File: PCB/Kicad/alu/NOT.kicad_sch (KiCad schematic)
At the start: 3 parts, among them U7 74LS04, U8 74LS04, U9 74LS04

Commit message: UPDATE
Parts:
- removed unit 6 of U9
- removed unit 5 of U9
- added C14, C15, C16: 10n, symbol Device:C
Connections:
- net GND: now also C14.2, C15.2, C16.2
- net VCC: now also C14.1, C15.1, C16.1
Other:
- moved on the sheet: U7G, U9G

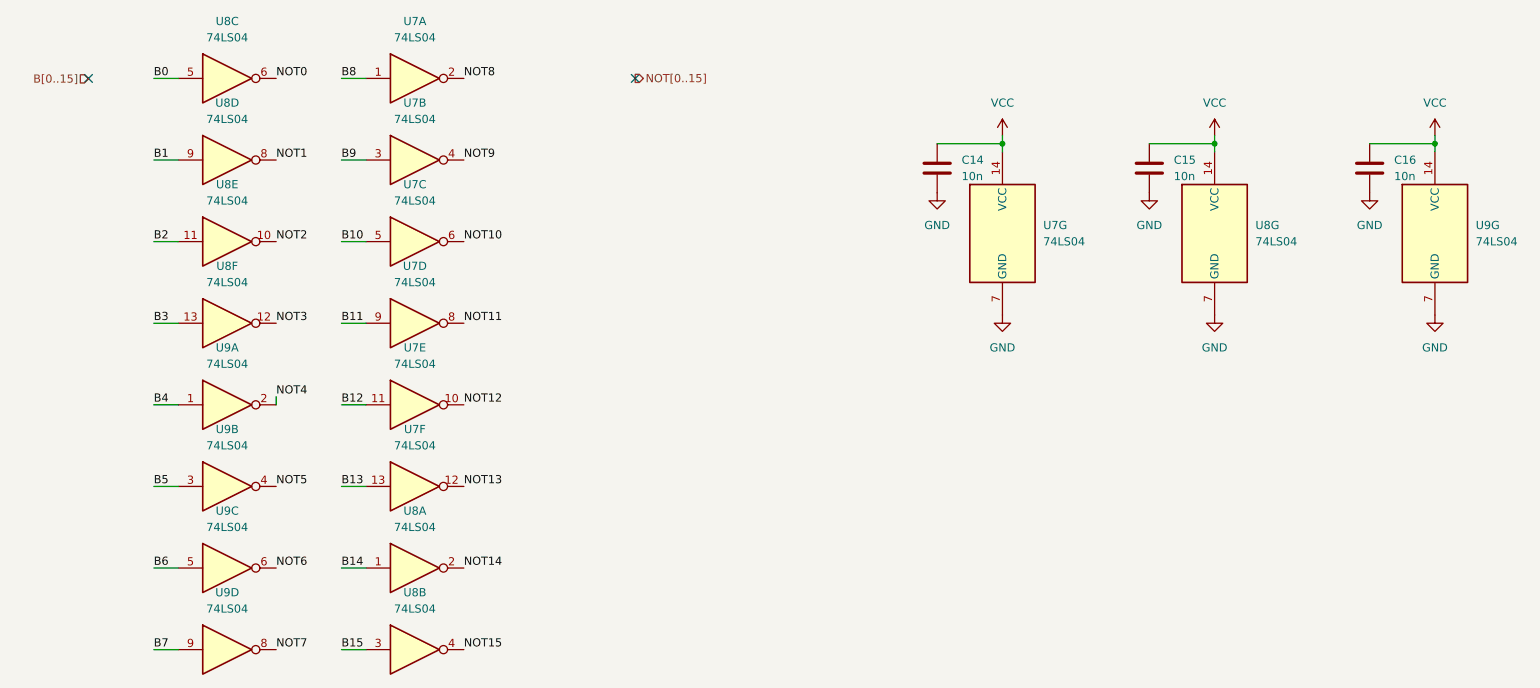
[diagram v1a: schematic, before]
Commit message: LEDs added
REGISTER.kicad_sch LEDs added to both REG_A and REG_B
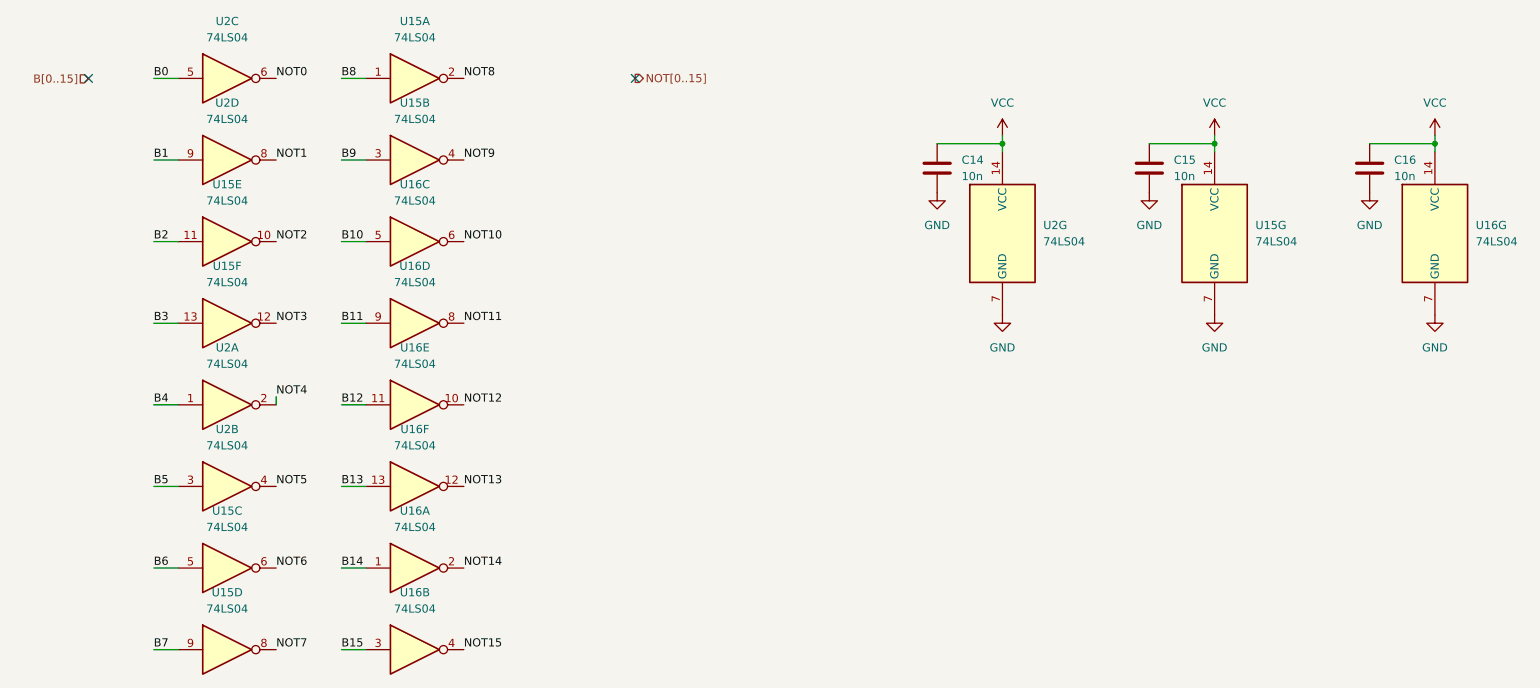
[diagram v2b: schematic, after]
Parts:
- renumbered U9 to U15, U7 to U15, U8 to U15, U7 to U16, U9 to U16, U8 to U16, U7 to U2, U8 to U2, U9 to U2
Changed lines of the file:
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@@
 		(dnp no)
 		(fields_autoplaced yes)
-		(property "Reference" "U7"
+		(property "Reference" "U2"
 			(at 199.39 45.7199 0)
 			(effects
@@
 			(project ""
 				(path "/2f66781e-a1af-4159-bccc-5b52a490afb6/f62161c6-7864-4502-bacc-9a62f524bb8c"
-					(reference "U7")
+					(reference "U2")
 					(unit 7)
 				)
@@
 		(dnp no)
 		(fields_autoplaced yes)
-		(property "Reference" "U7"
+		(property "Reference" "U16"
 			(at 101.6 52.07 0)
 			(effects
@@
 			(project ""
 				(path "/2f66781e-a1af-4159-bccc-5b52a490afb6/f62161c6-7864-4502-bacc-9a62f524bb8c"
-					(reference "U7")
+					(reference "U16")
 					(unit 4)
 				)
@@
 		(dnp no)
 		(fields_autoplaced yes)
-		(property "Reference" "#PWR028"
+		(property "Reference" "#PWR066"
 			(at 193.04 66.04 0)
 			(effects
@@
 			(project ""
 				(path "/2f66781e-a1af-4159-bccc-5b52a490afb6/f62161c6-7864-4502-bacc-9a62f524bb8c"
-					(reference "#PWR028")
+					(reference "#PWR066")
 					(unit 1)
 				)
@@
 		(dnp no)
 		(fields_autoplaced yes)
-		(property "Reference" "U9"
+		(property "Reference" "U15"
 			(at 72.39 102.87 0)
 			(effects
@@
 			(project "alu"
 				(path "/2f66781e-a1af-4159-bccc-5b52a490afb6/f62161c6-7864-4502-bacc-9a62f524bb8c"
-					(reference "U9")
+					(reference "U15")
 					(unit 4)
 				)
@@
 		(dnp no)
 		(fields_autoplaced yes)
-		(property "Reference" "U8"
+		(property "Reference" "U2"
 			(at 72.39 26.67 0)
 			(effects
@@
 			(project "alu"
 				(path "/2f66781e-a1af-4159-bccc-5b52a490afb6/f62161c6-7864-4502-bacc-9a62f524bb8c"
-					(reference "U8")
+					(reference "U2")
 					(unit 4)
 				)
@@
 		(dnp no)
 		(fields_autoplaced yes)
-		(property "Reference" "U9"
+		(property "Reference" "U16"
 			(at 266.7 45.7199 0)
 			(effects
@@
 			(project "alu"
 				(path "/2f66781e-a1af-4159-bccc-5b52a490afb6/f62161c6-7864-4502-bacc-9a62f524bb8c"
-					(reference "U9")
+					(reference "U16")
 					(unit 7)
 				)
@@
 		(dnp no)
 		(fields_autoplaced yes)
-		(property "Reference" "U7"
+		(property "Reference" "U16"
 			(at 101.6 39.37 0)
 			(effects
@@
 			(project ""
 				(path "/2f66781e-a1af-4159-bccc-5b52a490afb6/f62161c6-7864-4502-bacc-9a62f524bb8c"
-					(reference "U7")
+					(reference "U16")
 					(unit 3)
 				)
@@
 		(dnp no)
 		(fields_autoplaced yes)
-		(property "Reference" "#PWR0226"
+		(property "Reference" "#PWR070"
 			(at 250.19 46.99 0)
 			(effects
@@
 			(project "alu"
 				(path "/2f66781e-a1af-4159-bccc-5b52a490afb6/f62161c6-7864-4502-bacc-9a62f524bb8c"
-					(reference "#PWR0226")
+					(reference "#PWR070")
 					(unit 1)
 				)
@@
 		(dnp no)
 		(fields_autoplaced yes)
-		(property "Reference" "#PWR0224"
+		(property "Reference" "#PWR064"
 			(at 182.88 46.99 0)
 			(effects
@@
 			(project "alu"
 				(path "/2f66781e-a1af-4159-bccc-5b52a490afb6/f62161c6-7864-4502-bacc-9a62f524bb8c"
-					(reference "#PWR0224")
+					(reference "#PWR064")
 					(unit 1)
 				)
@@
 		(dnp no)
 		(fields_autoplaced yes)
-		(property "Reference" "U7"
+		(property "Reference" "U16"
 			(at 101.6 77.47 0)
 			(effects
@@
 			(project ""
 				(path "/2f66781e-a1af-4159-bccc-5b52a490afb6/f62161c6-7864-4502-bacc-9a62f524bb8c"
-					(reference "U7")
+					(reference "U16")
 					(unit 6)
 				)
@@
 		(dnp no)
 		(fields_autoplaced yes)
-		(property "Reference" "#PWR027"
+		(property "Reference" "#PWR071"
 			(at 260.35 35.56 0)
 			(effects
@@
 			(project "alu"
 				(path "/2f66781e-a1af-4159-bccc-5b52a490afb6/f62161c6-7864-4502-bacc-9a62f524bb8c"
-					(reference "#PWR027")
+					(reference "#PWR071")
 					(unit 1)
 				)
@@
 		(dnp no)
 		(fields_autoplaced yes)
-		(property "Reference" "#PWR0225"
+		(property "Reference" "#PWR067"
 			(at 215.9 46.99 0)
 			(effects
@@
 			(project "alu"
 				(path "/2f66781e-a1af-4159-bccc-5b52a490afb6/f62161c6-7864-4502-bacc-9a62f524bb8c"
-					(reference "#PWR0225")
+					(reference "#PWR067")
 					(unit 1)
 				)
@@
 		(dnp no)
 		(fields_autoplaced yes)
-		(property "Reference" "#PWR026"
+		(property "Reference" "#PWR068"
 			(at 226.06 35.56 0)
 			(effects
@@
 			(project "alu"
 				(path "/2f66781e-a1af-4159-bccc-5b52a490afb6/f62161c6-7864-4502-bacc-9a62f524bb8c"
-					(reference "#PWR026")
+					(reference "#PWR068")
 					(unit 1)
 				)
@@
 		(dnp no)
 		(fields_autoplaced yes)
-		(property "Reference" "U7"
+		(property "Reference" "U15"
 			(at 101.6 13.97 0)
 			(effects
@@
 			(project ""
 				(path "/2f66781e-a1af-4159-bccc-5b52a490afb6/f62161c6-7864-4502-bacc-9a62f524bb8c"
-					(reference "U7")
+					(reference "U15")
 					(unit 1)
 				)
@@
 		(dnp no)
 		(fields_autoplaced yes)
-		(property "Reference" "U9"
+		(property "Reference" "U15"
 			(at 72.39 90.17 0)
 			(effects
@@
 			(project "alu"
 				(path "/2f66781e-a1af-4159-bccc-5b52a490afb6/f62161c6-7864-4502-bacc-9a62f524bb8c"
-					(reference "U9")
+					(reference "U15")
 					(unit 3)
 				)
@@
 		(dnp no)
 		(fields_autoplaced yes)
-		(property "Reference" "U7"
+		(property "Reference" "U16"
 			(at 101.6 64.77 0)
 			(effects
@@
 			(project ""
 				(path "/2f66781e-a1af-4159-bccc-5b52a490afb6/f62161c6-7864-4502-bacc-9a62f524bb8c"
-					(reference "U7")
+					(reference "U16")
 					(unit 5)
 				)
@@
 		(dnp no)
 		(fields_autoplaced yes)
-		(property "Reference" "U9"
+		(property "Reference" "U2"
 			(at 72.39 64.77 0)
 			(effects
@@
 			(project "alu"
 				(path "/2f66781e-a1af-4159-bccc-5b52a490afb6/f62161c6-7864-4502-bacc-9a62f524bb8c"
-					(reference "U9")
+					(reference "U2")
 					(unit 1)
 				)
@@
 		(dnp no)
 		(fields_autoplaced yes)
-		(property "Reference" "U8"
+		(property "Reference" "U2"
 			(at 72.39 13.97 0)
 			(effects
@@
 			(project "alu"
 				(path "/2f66781e-a1af-4159-bccc-5b52a490afb6/f62161c6-7864-4502-bacc-9a62f524bb8c"
-					(reference "U8")
+					(reference "U2")
 					(unit 3)
 				)
@@
 		(dnp no)
 		(fields_autoplaced yes)
-		(property "Reference" "U8"
+		(property "Reference" "U15"
 			(at 232.41 45.7199 0)
 			(effects
@@
 			(project "alu"
 				(path "/2f66781e-a1af-4159-bccc-5b52a490afb6/f62161c6-7864-4502-bacc-9a62f524bb8c"
-					(reference "U8")
+					(reference "U15")
 					(unit 7)
 				)
@@
 		(dnp no)
 		(fields_autoplaced yes)
-		(property "Reference" "U8"
+		(property "Reference" "U15"
 			(at 72.39 39.37 0)
 			(effects
@@
 			(project "alu"
 				(path "/2f66781e-a1af-4159-bccc-5b52a490afb6/f62161c6-7864-4502-bacc-9a62f524bb8c"
-					(reference "U8")
+					(reference "U15")
 					(unit 5)
 				)
@@
 		(dnp no)
 		(fields_autoplaced yes)
-		(property "Reference" "U7"
+		(property "Reference" "U15"
 			(at 101.6 26.67 0)
 			(effects
@@
 			(project ""
 				(path "/2f66781e-a1af-4159-bccc-5b52a490afb6/f62161c6-7864-4502-bacc-9a62f524bb8c"
-					(reference "U7")
+					(reference "U15")
 					(unit 2)
 				)
@@
 		(dnp no)
 		(fields_autoplaced yes)
-		(property "Reference" "U8"
+		(property "Reference" "U16"
 			(at 101.6 102.87 0)
 			(effects
@@
 			(project "alu"
 				(path "/2f66781e-a1af-4159-bccc-5b52a490afb6/f62161c6-7864-4502-bacc-9a62f524bb8c"
-					(reference "U8")
+					(reference "U16")
 					(unit 2)
 				)
@@
 		(dnp no)
 		(fields_autoplaced yes)
-		(property "Reference" "#PWR029"
+		(property "Reference" "#PWR069"
 			(at 226.06 66.04 0)
 			(effects
@@
 			(project "alu"
 				(path "/2f66781e-a1af-4159-bccc-5b52a490afb6/f62161c6-7864-4502-bacc-9a62f524bb8c"
-					(reference "#PWR029")
+					(reference "#PWR069")
 					(unit 1)
 				)
@@
 		(dnp no)
 		(fields_autoplaced yes)
-		(property "Reference" "#PWR025"
+		(property "Reference" "#PWR065"
 			(at 193.04 35.56 0)
 			(effects
@@
 			(project ""
 				(path "/2f66781e-a1af-4159-bccc-5b52a490afb6/f62161c6-7864-4502-bacc-9a62f524bb8c"
-					(reference "#PWR025")
+					(reference "#PWR065")
 					(unit 1)
 				)
@@
 		(dnp no)
 		(fields_autoplaced yes)
-		(property "Reference" "U8"
+		(property "Reference" "U15"
 			(at 72.39 52.07 0)
 			(effects
@@
 			(project "alu"
 				(path "/2f66781e-a1af-4159-bccc-5b52a490afb6/f62161c6-7864-4502-bacc-9a62f524bb8c"
-					(reference "U8")
+					(reference "U15")
 					(unit 6)
 				)
@@
 		(dnp no)
 		(fields_autoplaced yes)
-		(property "Reference" "#PWR030"
+		(property "Reference" "#PWR072"
 			(at 260.35 66.04 0)
 			(effects
@@
 			(project "alu"
 				(path "/2f66781e-a1af-4159-bccc-5b52a490afb6/f62161c6-7864-4502-bacc-9a62f524bb8c"
-					(reference "#PWR030")
+					(reference "#PWR072")
 					(unit 1)
 				)
@@
 		(dnp no)
 		(fields_autoplaced yes)
-		(property "Reference" "U9"
+		(property "Reference" "U2"
 			(at 72.39 77.47 0)
 			(effects
@@
 			(project "alu"
 				(path "/2f66781e-a1af-4159-bccc-5b52a490afb6/f62161c6-7864-4502-bacc-9a62f524bb8c"
-					(reference "U9")
+					(reference "U2")
 					(unit 2)
 				)
@@
 		(dnp no)
 		(fields_autoplaced yes)
-		(property "Reference" "U8"
+		(property "Reference" "U16"
 			(at 101.6 90.17 0)
 			(effects
@@
 			(project "alu"
 				(path "/2f66781e-a1af-4159-bccc-5b52a490afb6/f62161c6-7864-4502-bacc-9a62f524bb8c"
-					(reference "U8")
+					(reference "U16")
 					(unit 1)
 				)

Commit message: Footprints, PCB update
Added footprints to all components, updated the PCB with the schematic
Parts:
- C14, C15, C16: footprint (none) -> Capacitor_SMD:C_0603_1608Metric
- U15, U16, U2: footprint (none) -> Package_SO:SOIC-14_3.9x8.7mm_P1.27mm
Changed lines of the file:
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@@
 			)
 		)
-		(property "Footprint" ""
+		(property "Footprint" "Package_SO:SOIC-14_3.9x8.7mm_P1.27mm"
 			(at 193.04 46.99 0)
 			(effects
@@
 			)
 		)
-		(property "Footprint" ""
+		(property "Footprint" "Package_SO:SOIC-14_3.9x8.7mm_P1.27mm"
 			(at 101.6 60.96 0)
 			(effects
@@
 			)
 		)
-		(property "Footprint" ""
+		(property "Footprint" "Package_SO:SOIC-14_3.9x8.7mm_P1.27mm"
 			(at 72.39 111.76 0)
 			(effects
@@
 			)
 		)
-		(property "Footprint" ""
+		(property "Footprint" "Package_SO:SOIC-14_3.9x8.7mm_P1.27mm"
 			(at 72.39 35.56 0)
 			(effects
@@
 			)
 		)
-		(property "Footprint" ""
+		(property "Footprint" "Package_SO:SOIC-14_3.9x8.7mm_P1.27mm"
 			(at 260.35 46.99 0)
 			(effects
@@
 			)
 		)
-		(property "Footprint" ""
+		(property "Footprint" "Package_SO:SOIC-14_3.9x8.7mm_P1.27mm"
 			(at 101.6 48.26 0)
 			(effects
@@
 			)
 		)
-		(property "Footprint" ""
+		(property "Footprint" "Package_SO:SOIC-14_3.9x8.7mm_P1.27mm"
 			(at 101.6 86.36 0)
 			(effects
@@
 			)
 		)
-		(property "Footprint" ""
+		(property "Footprint" "Package_SO:SOIC-14_3.9x8.7mm_P1.27mm"
 			(at 101.6 22.86 0)
 			(effects
@@
 			)
 		)
-		(property "Footprint" ""
+		(property "Footprint" "Package_SO:SOIC-14_3.9x8.7mm_P1.27mm"
 			(at 72.39 99.06 0)
 			(effects
@@
 			)
 		)
-		(property "Footprint" ""
+		(property "Footprint" "Package_SO:SOIC-14_3.9x8.7mm_P1.27mm"
 			(at 101.6 73.66 0)
 			(effects
@@
 			)
 		)
-		(property "Footprint" ""
+		(property "Footprint" "Package_SO:SOIC-14_3.9x8.7mm_P1.27mm"
 			(at 72.39 73.66 0)
 			(effects
@@
 			)
 		)
-		(property "Footprint" ""
+		(property "Footprint" "Package_SO:SOIC-14_3.9x8.7mm_P1.27mm"
 			(at 72.39 22.86 0)
 			(effects
@@
 			)
 		)
-		(property "Footprint" ""
+		(property "Footprint" "Package_SO:SOIC-14_3.9x8.7mm_P1.27mm"
 			(at 226.06 46.99 0)
 			(effects
@@
 			)
 		)
-		(property "Footprint" ""
+		(property "Footprint" "Capacitor_SMD:C_0603_1608Metric"
 			(at 216.8652 40.64 0)
 			(effects
@@
 			)
 		)
-		(property "Footprint" ""
+		(property "Footprint" "Package_SO:SOIC-14_3.9x8.7mm_P1.27mm"
 			(at 72.39 48.26 0)
 			(effects
@@
 			)
 		)
-		(property "Footprint" ""
+		(property "Footprint" "Package_SO:SOIC-14_3.9x8.7mm_P1.27mm"
 			(at 101.6 35.56 0)
 			(effects
@@
 			)
 		)
-		(property "Footprint" ""
+		(property "Footprint" "Package_SO:SOIC-14_3.9x8.7mm_P1.27mm"
 			(at 101.6 111.76 0)
 			(effects
@@
 			)
 		)
-		(property "Footprint" ""
+		(property "Footprint" "Capacitor_SMD:C_0603_1608Metric"
 			(at 183.8452 40.64 0)
 			(effects
@@
 			)
 		)
-		(property "Footprint" ""
+		(property "Footprint" "Package_SO:SOIC-14_3.9x8.7mm_P1.27mm"
 			(at 72.39 60.96 0)
 			(effects
@@
 			)
 		)
-		(property "Footprint" ""
+		(property "Footprint" "Package_SO:SOIC-14_3.9x8.7mm_P1.27mm"
 			(at 72.39 86.36 0)
 			(effects
@@
 			)
 		)
-		(property "Footprint" ""
+		(property "Footprint" "Capacitor_SMD:C_0603_1608Metric"
 			(at 251.1552 40.64 0)
 			(effects
@@
 			)
 		)
-		(property "Footprint" ""
+		(property "Footprint" "Package_SO:SOIC-14_3.9x8.7mm_P1.27mm"
 			(at 101.6 99.06 0)
 			(effects

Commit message: ALU Pcb update
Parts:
- C14, C15, C16: value 10n -> 100nF; footprint Capacitor_SMD:C_0603_1608Metric -> Capacitor_SMD:C_0402_1005Metric
- U15, U16, U2: value 74LS04 -> 7404; footprint Package_SO:SOIC-14_3.9x8.7mm_P1.27mm -> Package_SO:SO-14_3.9x8.65mm_P1.27mm
